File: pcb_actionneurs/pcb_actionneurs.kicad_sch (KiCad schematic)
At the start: 23 parts, among them J1 USB_C_Receptacle_USB2.0_16P, J2 Conn_ST_STDC14, J3 1755736, U1 STM32G491KEU6

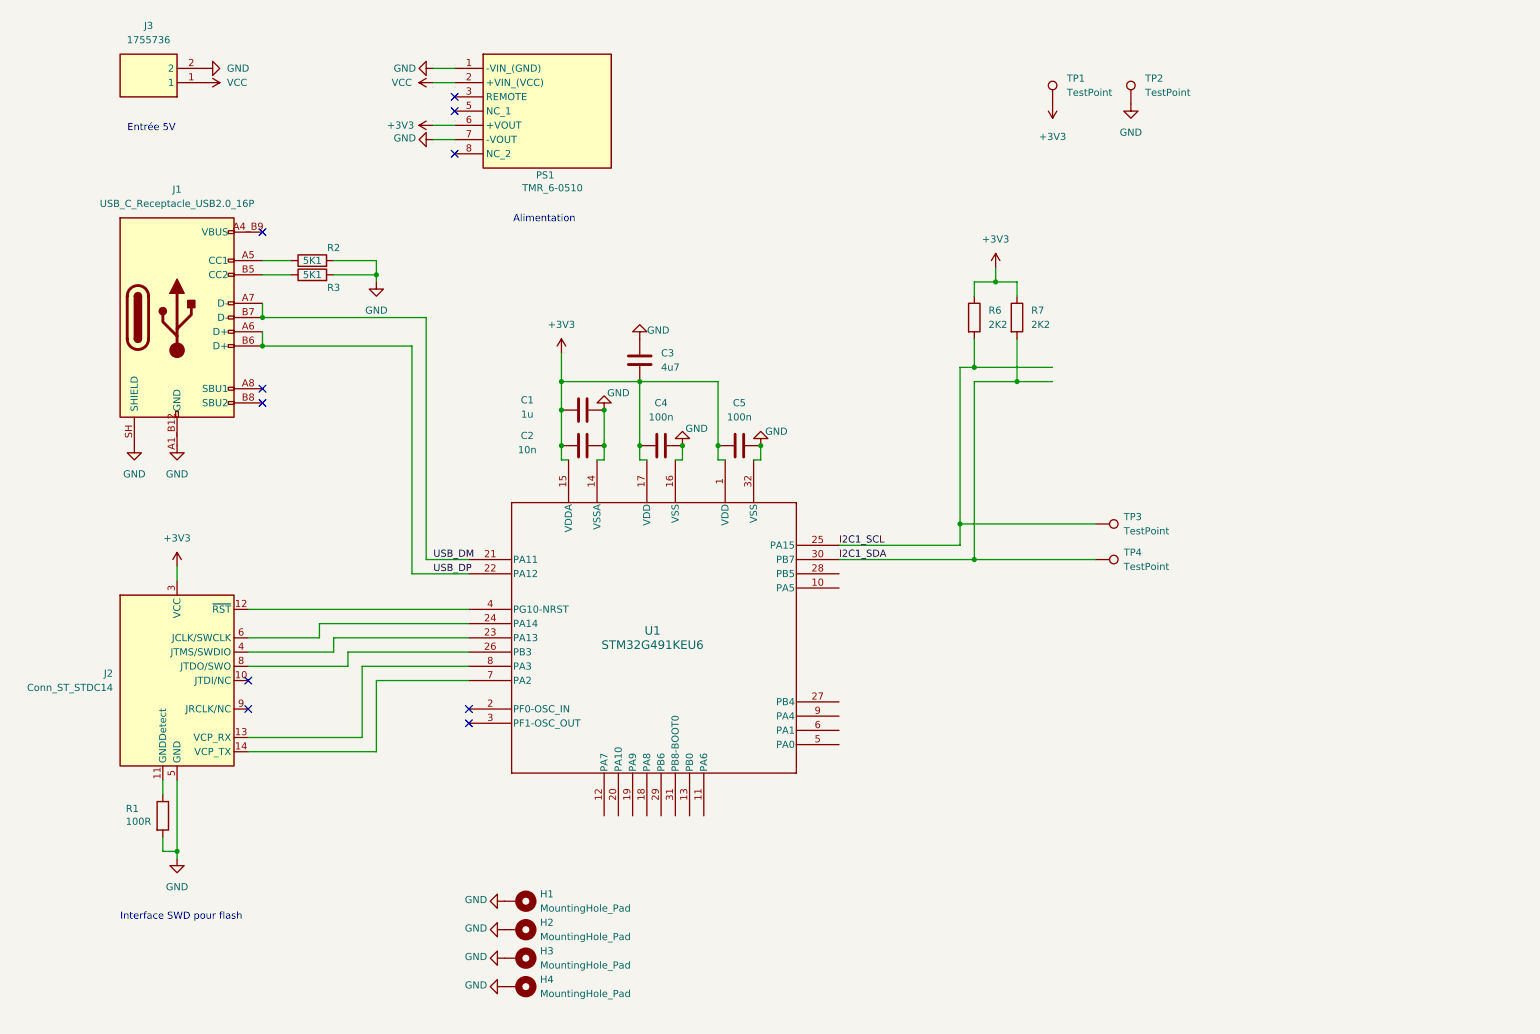
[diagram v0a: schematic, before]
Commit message: premier jet routage pcb actionneurs, encore des choses à faire
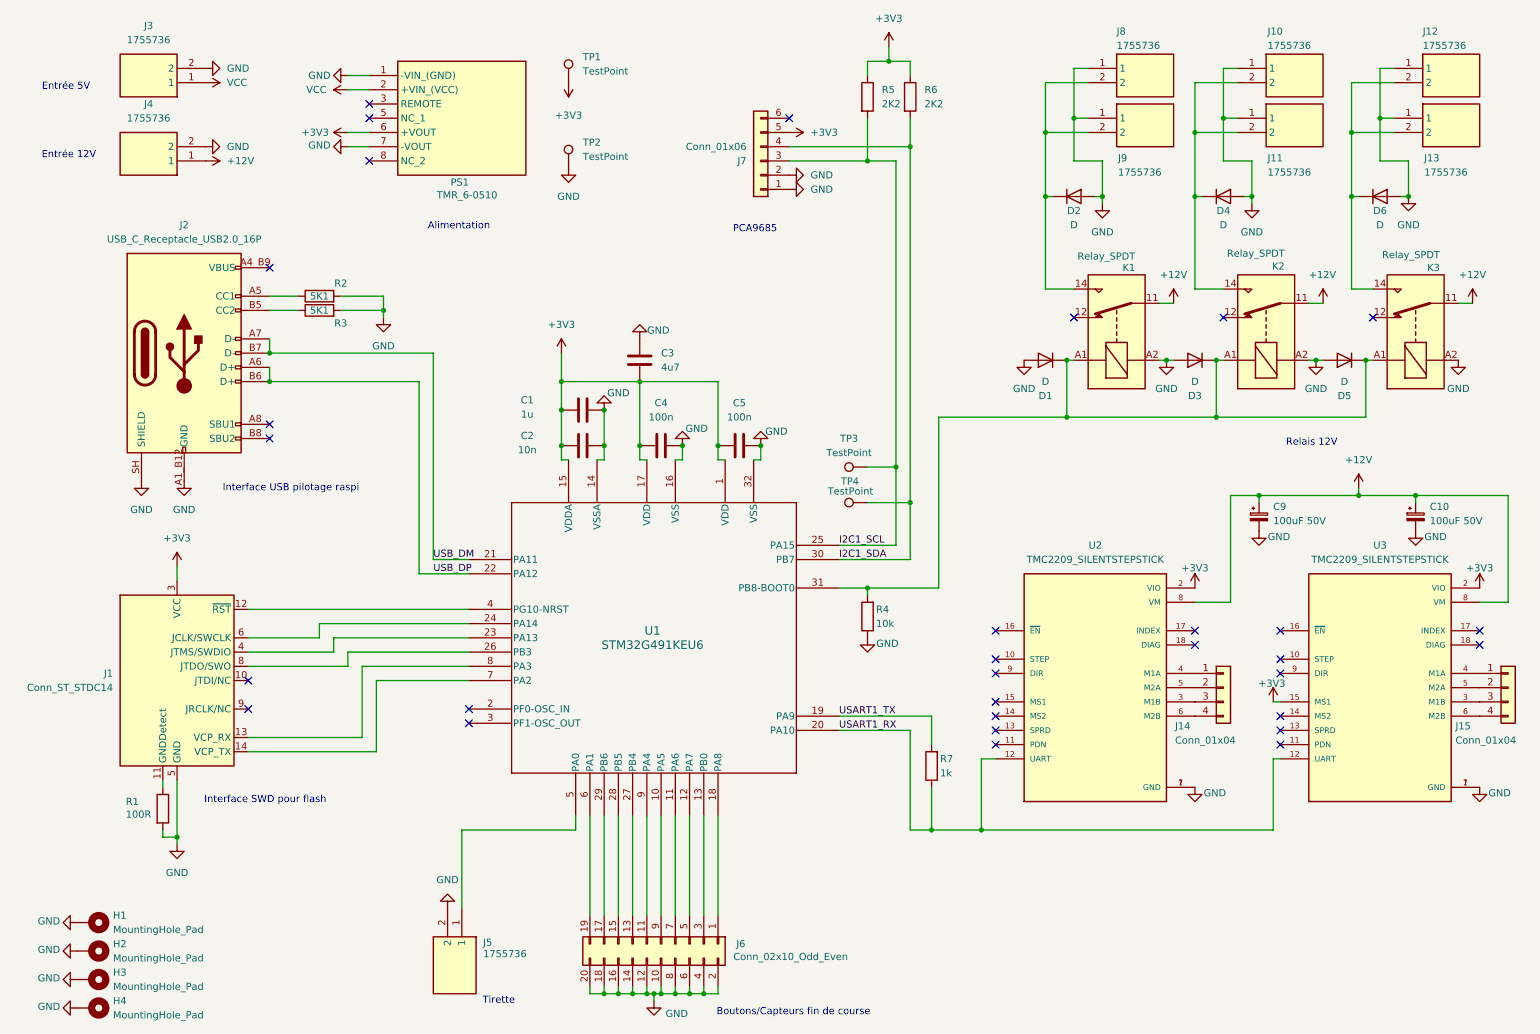
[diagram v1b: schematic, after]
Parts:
- added C10, C9: 100uF 50V, Capacitor_THT:CP_Radial_D8.0mm_P3.80mm, symbol Device:C_Polarized_Small
- added D1, D2, D3, D4, D5, D6: D, Diode_THT:D_DO-35_SOD27_P7.62mm_Horizontal, symbol Device:D
- added J10, J11, J12, J13, J4, J5, J8, J9: 1755736, Modelec:PhoenixContact_MSTBVA_2,5_2-G-5,08_1x02_P5.08mm_Vertical, symbol Modelec:1755736
- added J14, J15: Conn_01x04, Connector_PinHeader_2.54mm:PinHeader_1x04_P2.54mm_Vertical, symbol Connector_Generic:Conn_01x04
- added J6: Conn_02x10_Odd_Even, Connector_PinHeader_2.54mm:PinHeader_2x10_P2.54mm_Vertical, symbol Connector_Generic:Conn_02x10_Odd_Even
- added J7: Conn_01x06, Connector_PinHeader_2.54mm:PinHeader_1x06_P2.54mm_Vertical, symbol Connector_Generic:Conn_01x06
- added K1, K2, K3: Relay_SPDT, Relay_THT:Relay_SPDT_Finder_36.11, symbol Relay:Relay_SPDT
- added R4: 10k, Resistor_SMD:R_0805_2012Metric_Pad1.20x1.40mm_HandSolder, symbol Device:R
- added R7: 1k, Resistor_SMD:R_0805_2012Metric_Pad1.20x1.40mm_HandSolder, symbol Device:R
- added U2, U3: TMC2209_SILENTSTEPSTICK, Modelec:MODULE_TMC2209_SILENTSTEPSTICK, symbol Modelec:TMC2209_SILENTSTEPSTICK
- renumbered J2 to J1, J1 to J2, R6 to R5, R7 to R6
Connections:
- net +3V3: now also J7.5 (Pin_5), U2.2 (VIO), U3.15 (MS1), U3.2 (VIO)
- net GND: now also C10.2, C9.2, D1.2 (A), D2.2 (A), D3.2 (A), D4.2 (A), D5.2 (A), D6.2 (A), J10.1, J11.1, J12.1, J13.1, J4.2, J5.2, J6.10 (Pin_10), J6.12 (Pin_12), J6.14 (Pin_14), J6.16 (Pin_16), J6.18 (Pin_18), J6.2 (Pin_2), J6.20 (Pin_20), J6.4 (Pin_4), J6.6 (Pin_6), J6.8 (Pin_8), J7.1 (Pin_1), J7.2 (Pin_2), J8.1, J9.1, K1.A2, K2.A2, K3.A2, R4.1, U2.1 (GND), U2.7 (GND), U3.1 (GND), U3.7 (GND)
- net I2C1_SCL: now also J7.3 (Pin_3)
- net I2C1_SDA: now also J7.4 (Pin_4)
- net at U1.10 (PA5): now also J6.9 (Pin_9)
- net at U1.11 (PA6): now also J6.7 (Pin_7)
- net at U1.12 (PA7): now also J6.5 (Pin_5)
- net at U1.13 (PB0): now also J6.3 (Pin_3)
- net at U1.18 (PA8): now also J6.1 (Pin_1)
- net USART1_TX: now reaches U1.19 (PA9)
- net USART1_TX: now also R7.2
- net USART1_RX: now reaches U1.20 (PA10)
- net USART1_RX: now also R7.1, U2.12 (UART), U3.12 (UART)
- net at U1.27 (PB4): now also J6.13 (Pin_13)
- net at U1.28 (PB5): now also J6.15 (Pin_15)
- net at U1.29 (PB6): now also J6.17 (Pin_17)
- net at U1.31 (PB8-BOOT0): now also D1.1 (K), D3.1 (K), D5.1 (K), K1.A1, K2.A1, K3.A1, R4.2
- net at U1.5 (PA0): now also J5.1
- net at U1.6 (PA1): now also J6.19 (Pin_19)
- net at U1.9 (PA4): now also J6.11 (Pin_11)
- new net: D6.1 (K), J12.2, J13.2, K3.14
- new net: D4.1 (K), J10.2, J11.2, K2.14
- new net: J15.3 (Pin_3), U3.3 (M1B)
- new net: J15.1 (Pin_1), U3.4 (M1A)
- new net: J15.2 (Pin_2), U3.5 (M2A)
- new net: J15.4 (Pin_4), U3.6 (M2B)
- new net: J14.3 (Pin_3), U2.3 (M1B)
- new net: J14.1 (Pin_1), U2.4 (M1A)
- new net: J14.2 (Pin_2), U2.5 (M2A)
- new net: J14.4 (Pin_4), U2.6 (M2B)
- new net: D2.1 (K), J8.2, J9.2, K1.14
- new net +12V: C10.1, C9.1, J4.1, K1.11, K2.11, K3.11, U2.8 (VM), U3.8 (VM)
- no-connect marks 10 -> 31
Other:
- note added: "Boutons/Capteurs fin de course"
- note added: "Entrée 12V"
- note added: "Interface USB pilotage raspi"
- note added: "PCA9685"
- note added: "Relais 12V"
- note added: "Tirette"
- moved on the sheet: H1, H2, H3, H4, J2, PS1, R1, R2, R3, R5, R6, TP1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

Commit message: Ajout BAU servo PAMI, finitions PCB Actionneurs, fichier fab stencil. Version commandée PAMI & Actionneurs
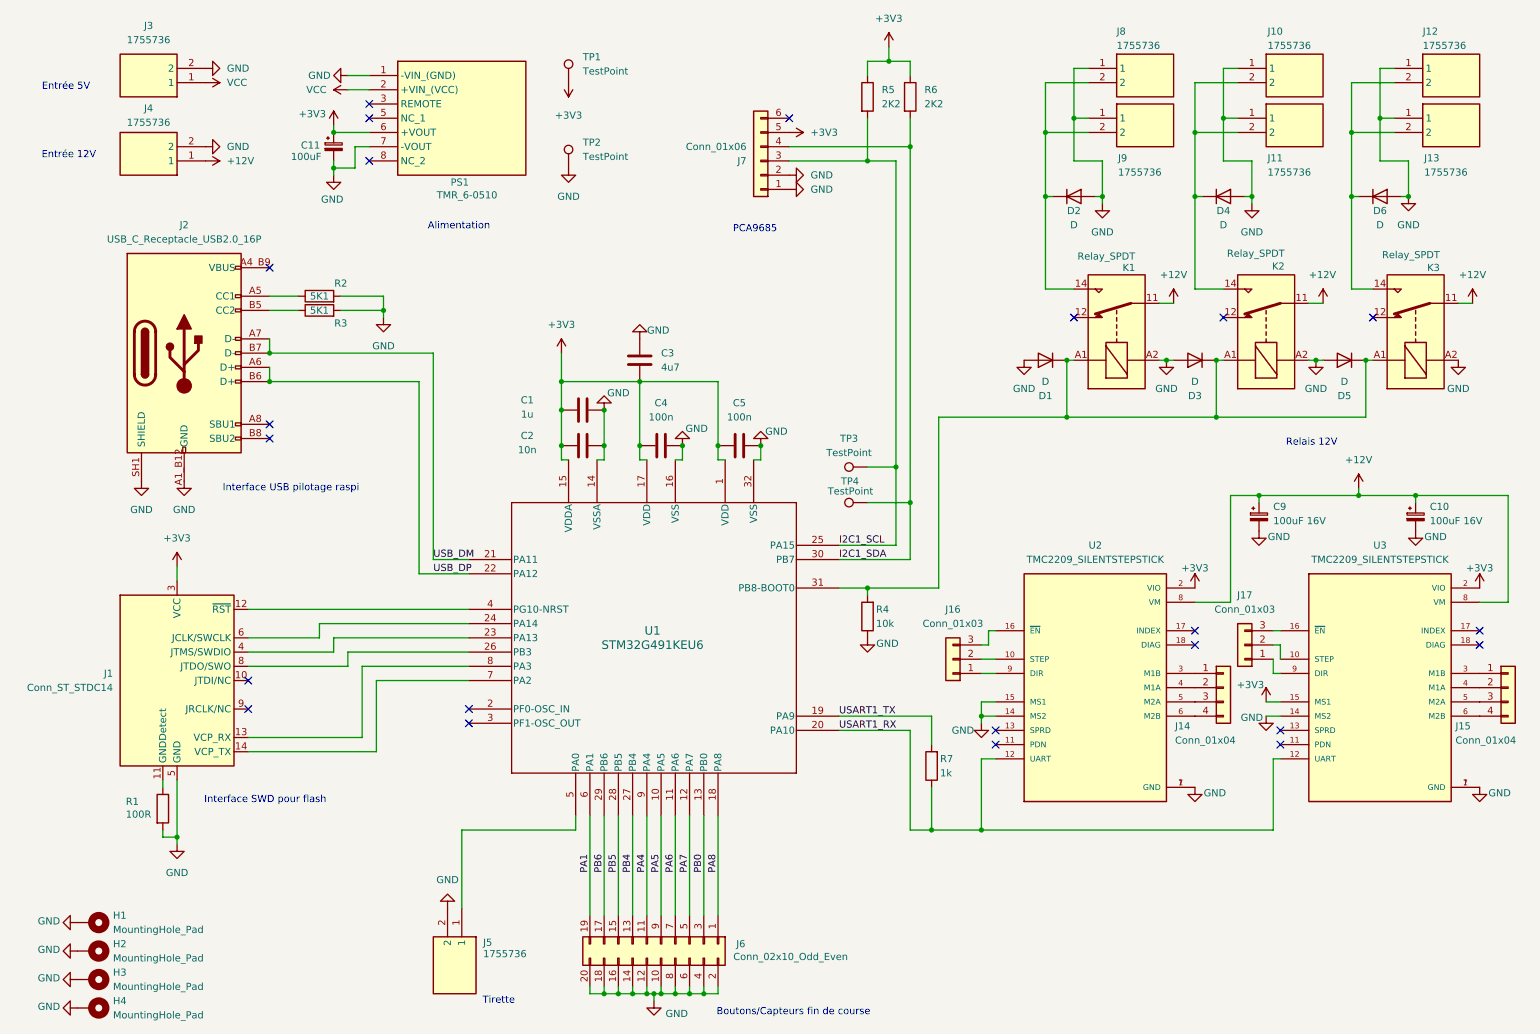
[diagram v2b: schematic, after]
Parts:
- added C11: 100uF, Capacitor_THT:C_Radial_D6.3mm_H11.0mm_P2.50mm, symbol Device:C_Polarized_Small
- added J16, J17: Conn_01x03, Connector_PinHeader_2.54mm:PinHeader_1x03_P2.54mm_Vertical, symbol Connector_Generic:Conn_01x03
- C10, C9: value 100uF 50V -> 100uF 16V; footprint Capacitor_THT:CP_Radial_D8.0mm_P3.80mm -> w_capacitors:CP_6.3x11mm_horiz-L
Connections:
- net +3V3: now also C11.1
- net GND: now also J2.SH1 (SHIELD), J2.SH2, J2.SH3, J2.SH4, U2.14 (MS2), U2.15 (MS1), U3.14 (MS2), C11.2; no longer J2.SH (SHIELD)
- net PA8: now reaches J6.1 (Pin_1), U1.18 (PA8)
- net PA4: now reaches J6.11 (Pin_11), U1.9 (PA4)
- net PB4: now reaches J6.13 (Pin_13), U1.27 (PB4)
- net PB5: now reaches J6.15 (Pin_15), U1.28 (PB5)
- net PB6: now reaches J6.17 (Pin_17), U1.29 (PB6)
- net PA1: now reaches J6.19 (Pin_19), U1.6 (PA1)
- net PB0: now reaches J6.3 (Pin_3), U1.13 (PB0)
- net PA7: now reaches J6.5 (Pin_5), U1.12 (PA7)
- net PA6: now reaches J6.7 (Pin_7), U1.11 (PA6)
- net PA5: now reaches J6.9 (Pin_9), U1.10 (PA5)
- net at U3.10 (STEP): now also J17.2 (Pin_2)
- net at U3.16 (~{EN}): now also J17.3 (Pin_3)
- net at U3.3 (M1B): now also J15.1 (Pin_1); no longer J15.3 (Pin_3)
- net at U3.4 (M1A): now also J15.2 (Pin_2); no longer J15.1 (Pin_1)
- net at U3.5 (M2A): now also J15.3 (Pin_3); no longer J15.2 (Pin_2)
- net at U3.9 (DIR): now also J17.1 (Pin_1)
- net at U2.10 (STEP): now also J16.2 (Pin_2)
- net at U2.16 (~{EN}): now also J16.3 (Pin_3)
- net at U2.3 (M1B): now also J14.1 (Pin_1); no longer J14.3 (Pin_3)
- net at U2.4 (M1A): now also J14.2 (Pin_2); no longer J14.1 (Pin_1)
- net at U2.5 (M2A): now also J14.3 (Pin_3); no longer J14.2 (Pin_2)
- net at U2.9 (DIR): now also J16.1 (Pin_1)
- no-connect marks 31 -> 22
